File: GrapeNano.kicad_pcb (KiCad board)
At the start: 2 copper layers, 18.3 x 43.7 mm, 31 parts, among them P1 USB_OTG, P2 ICSP, SW1 SW_Push, U1 LM1117-5.0, U2 CH340G, U3 ATMEGA328P-AU, Y1 12MHz, Y2 16Mhz

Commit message: Enrutando
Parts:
- moved F1 6.58 mm to (152.1, 120.6), turned to 90 degrees
- moved Y1 3.54 mm to (160.3, 116.3), turned to 180 degrees
- moved D1 1.78 mm to (154.9, 87.5)
- moved D2 1.78 mm to (156.7, 87.5)
- moved D4 1.78 mm to (160.3, 87.5)
- moved D5 1.78 mm to (158.5, 87.5)
- moved R1 1.78 mm to (154.9, 90.8)
- moved R2 1.78 mm to (156.7, 90.8)
- moved R6 1.78 mm to (160.3, 90.8)
- moved R7 1.78 mm to (158.5, 90.8)
- moved R5 1.53 mm to (161.5, 94.2)
- moved SW1 1.52 mm to (157.5, 94.0)
- moved Y2 0.95 mm to (152.8, 98.4)
- moved P2 0.89 mm to (154.9, 83.8)
- moved D3 0.32 mm to (154.9, 116.4)
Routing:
- net +5V: track 62.2 -> 23.6 mm, vias 3 -> 2
- net A7: track 0.00 -> 27.3 mm
- net D1-TX: track 28.7 -> 8.84 mm, vias 2 -> 0
- net VUSB: track 21.0 -> 7.76 mm, vias 1 -> 0
- net D0-RX: track 20.8 -> 8.86 mm, vias 1 -> 0
- net Net-(C1-Pad2): track 8.67 -> 0.00 mm, vias 2 -> 0
- net GND: track 0.00 -> 8.64 mm, vias 0 -> 3
- net Net-(P1-Pad2): track 9.07 -> 16.5 mm
- net Net-(C6-Pad1): track 17.0 -> 12.3 mm
- net A6: track 0.00 -> 3.25 mm, vias 0 -> 1
- net RESET: track 30.2 -> 33.2 mm
- net DTR: track 2.32 -> 0.00 mm
- net Net-(F1-Pad2): track 5.60 -> 7.73 mm
- net Net-(U2-Pad7): track 2.58 -> 4.55 mm
- net D3: track 9.08 -> 10.8 mm
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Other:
- board size 18.3 x 43.7 mm -> 18.5 x 43.7 mm

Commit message: 4 nets
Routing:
- net D13-SCK: track 11.5 -> 68.0 mm, vias 0 -> 1
- net +5V: track 23.6 -> 71.6 mm, vias 2 -> 4
- net RESET: track 33.2 -> 75.1 mm, vias 0 -> 2
- net D1-TX: track 8.84 -> 46.9 mm, vias 0 -> 1
- net D12-MISO: track 11.6 -> 49.1 mm
- net D11-MOSI: track 9.35 -> 43.6 mm, vias 0 -> 1
- net D0-RX: track 8.86 -> 41.9 mm, vias 0 -> 4
- net VUSB: track 7.76 -> 32.5 mm, vias 0 -> 1
- net GND: track 8.64 -> 33.3 mm, vias 3 -> 12
- net A6: track 3.25 -> 21.8 mm, vias 1 -> 2
- net VIN: track 0.00 -> 15.6 mm
- net Net-(C1-Pad2): track 0.00 -> 8.04 mm
- net Net-(C6-Pad1): track 12.3 -> 18.6 mm
- net DTR: track 0.00 -> 2.32 mm
- net Net-(P1-Pad3): track 9.65 -> 10.6 mm
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
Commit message: enrutando
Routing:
- net (no net): track 0.00 -> 5.44 mm, vias 2 -> 1
- net GND: track 33.3 -> 36.5 mm
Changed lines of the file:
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@@
     (thickness 1.6)
     (drawings 9)
-    (tracks 450)
+    (tracks 458)
     (zones 0)
     (modules 31)
@@
   )
   (via (at 150.622 92.202) (size 0.8) (drill 0.4) (layers F.Cu B.Cu) (net 0))
-  (via (at 151.638 85.598) (size 0.8) (drill 0.4) (layers F.Cu B.Cu) (net 0))
+  (segment (start 156.972 80.01) (end 156.718 80.01) (width 0.25) (layer B.Cu) (net 0))
+  (segment (start 156.718 80.01) (end 157.734 80.01) (width 0.25) (layer B.Cu) (net 0))
+  (segment (start 157.734 80.01) (end 158.242 80.01) (width 0.25) (layer B.Cu) (net 0))
+  (segment (start 156.718 80.01) (end 154.338094 80.01) (width 0.25) (layer B.Cu) (net 0))
+  (segment (start 151.638 87.941002) (end 152.146 88.449002) (width 0.25) (layer B.Cu) (net 0))
+  (segment (start 151.638 85.032315) (end 151.638 85.598) (width 0.25) (layer B.Cu) (net 0))
   (segment (start 160.011861 108.444047) (end 160.782 109.214186) (width 0.25) (layer F.Cu) (net 2) (status 10))
   (segment (start 160.782 109.214186) (end 160.782 109.63868) (width 0.25) (layer F.Cu) (net 2))
@@
   (segment (start 156.755152 96.545152) (end 156.73 96.52) (width 0.25) (layer B.Cu) (net 5))
   (segment (start 157.204846 96.545152) (end 156.755152 96.545152) (width 0.25) (layer B.Cu) (net 5))
+  (segment (start 151.282499 89.371003) (end 151.478001 89.371003) (width 0.25) (layer B.Cu) (net 5))
+  (segment (start 149.637001 91.016501) (end 151.282499 89.371003) (width 0.25) (layer B.Cu) (net 5))
+  (segment (start 151.478001 89.371003) (end 151.954796 88.894208) (width 0.25) (layer B.Cu) (net 5))
   (segment (start 162.274603 106.181305) (end 164.877001 108.783703) (width 0.25) (layer F.Cu) (net 6) (status 30))
   (segment (start 164.877001 108.783703) (end 164.877001 108.796501) (width 0.25) (layer F.Cu) (net 6) (status 30))
@@
   (segment (start 155.69851 109.575417) (end 156.718 108.555927) (width 0.25) (layer F.Cu) (net 40))
   (via (at 156.718 108.458) (size 0.8) (drill 0.4) (layers F.Cu B.Cu) (net 40))
+  (segment (start 152.4 96.208998) (end 152.4 105.935002) (width 0.25) (layer B.Cu) (net 40))
+  (segment (start 152.4 105.935002) (end 153.662997 107.197999) (width 0.25) (layer B.Cu) (net 40))
+  (segment (start 153.662997 107.197999) (end 156.023684 107.197999) (width 0.25) (layer B.Cu) (net 40))
   (segment (start 156.718 107.892315) (end 156.718 108.458) (width 0.25) (layer B.Cu) (net 40))
+  (segment (start 152.146 95.954998) (end 152.4 96.208998) (width 0.25) (layer B.Cu) (net 40))
   (segment (start 156.023684 107.197999) (end 156.718 107.892315) (width 0.25) (layer B.Cu) (net 40))
-  (segment (start 153.662997 107.197999) (end 156.023684 107.197999) (width 0.25) (layer B.Cu) (net 40))
-  (segment (start 152.146 95.954998) (end 152.4 96.208998) (width 0.25) (layer B.Cu) (net 40))
+  (segment (start 152.146 90.678) (end 152.146 95.954998) (width 0.25) (layer B.Cu) (net 40))
   (segment (start 156.215199 86.608801) (end 152.146 90.678) (width 0.25) (layer B.Cu) (net 40))
-  (segment (start 152.4 96.208998) (end 152.4 105.935002) (width 0.25) (layer B.Cu) (net 40))
-  (segment (start 156.215199 82.544801) (end 156.215199 86.608801) (width 0.25) (layer B.Cu) (net 40))
-  (segment (start 152.146 90.678) (end 152.146 95.954998) (width 0.25) (layer B.Cu) (net 40))
-  (segment (start 157.48 81.28) (end 156.215199 82.544801) (width 0.25) (layer B.Cu) (net 40))
-  (segment (start 152.4 105.935002) (end 153.662997 107.197999) (width 0.25) (layer B.Cu) (net 40))
+  (segment (start 156.215199 82.544801) (end 157.48 81.28) (width 0.25) (layer B.Cu) (net 40))
+  (segment (start 156.215199 86.608801) (end 156.215199 82.544801) (width 0.25) (layer B.Cu) (net 40))
   (segment (start 162.1155 106.553) (end 162.2425 106.426) (width 0.25) (layer B.Cu) (net 41))
   (segment (start 160.053 106.553) (end 162.1155 106.553) (width 0.25) (layer B.Cu) (net 41))

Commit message: 1 net
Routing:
- net +5V: track 71.6 -> 81.0 mm, vias 4 -> 2
- net Net-(C6-Pad1): track 18.6 -> 23.9 mm, vias 0 -> 1
- net GND: track 36.5 -> 39.0 mm, vias 12 -> 14
- net (no net): track 5.44 -> 4.16 mm
- net D4: track 10.8 -> 11.9 mm
- net RESET: track 75.1 -> 76.0 mm, vias 2 -> 4

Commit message: Enrutado completo
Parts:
- moved C2 0.51 mm to (157.5, 96.0)
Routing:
- net GND: track 39.0 -> 46.2 mm, vias 14 -> 17
- net +5V: track 81.0 -> 79.5 mm
- net (no net): vias 1 -> 0

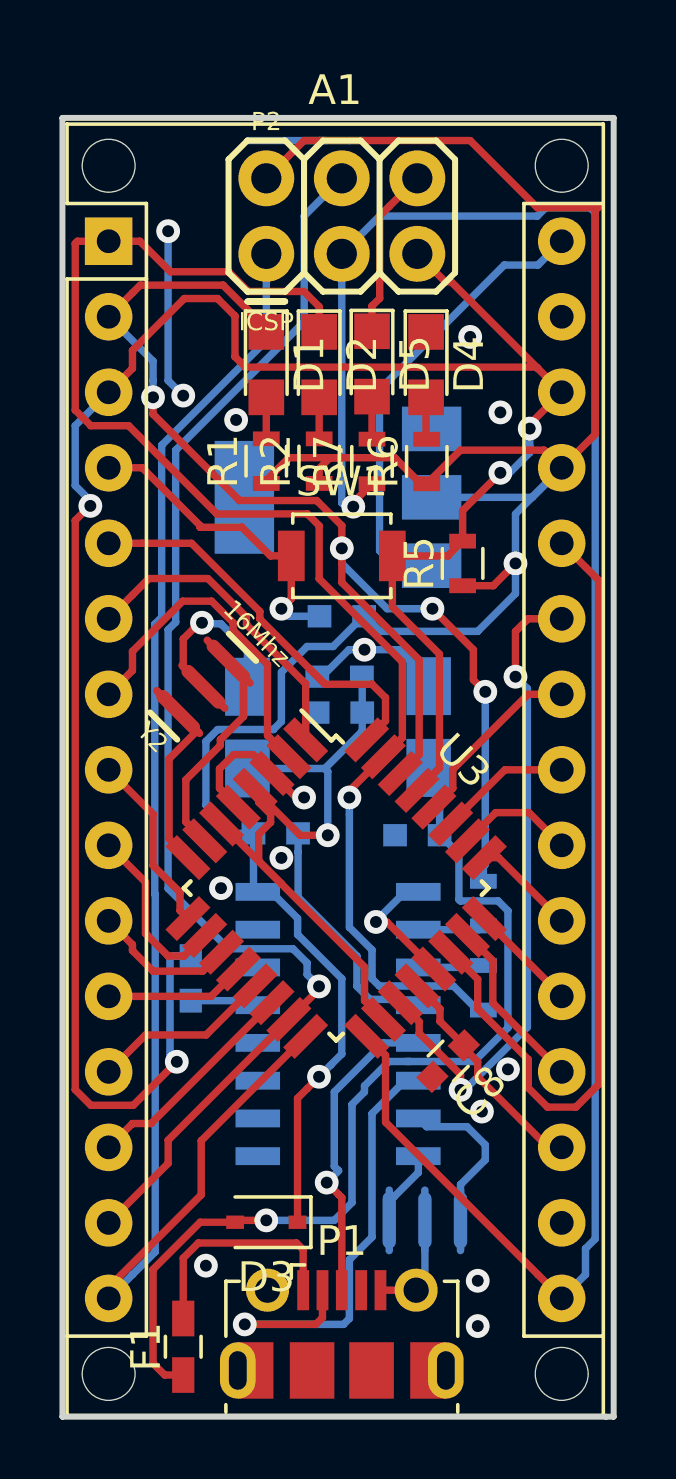
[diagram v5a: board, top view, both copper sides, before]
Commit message: CH340G cambiado por CH340C
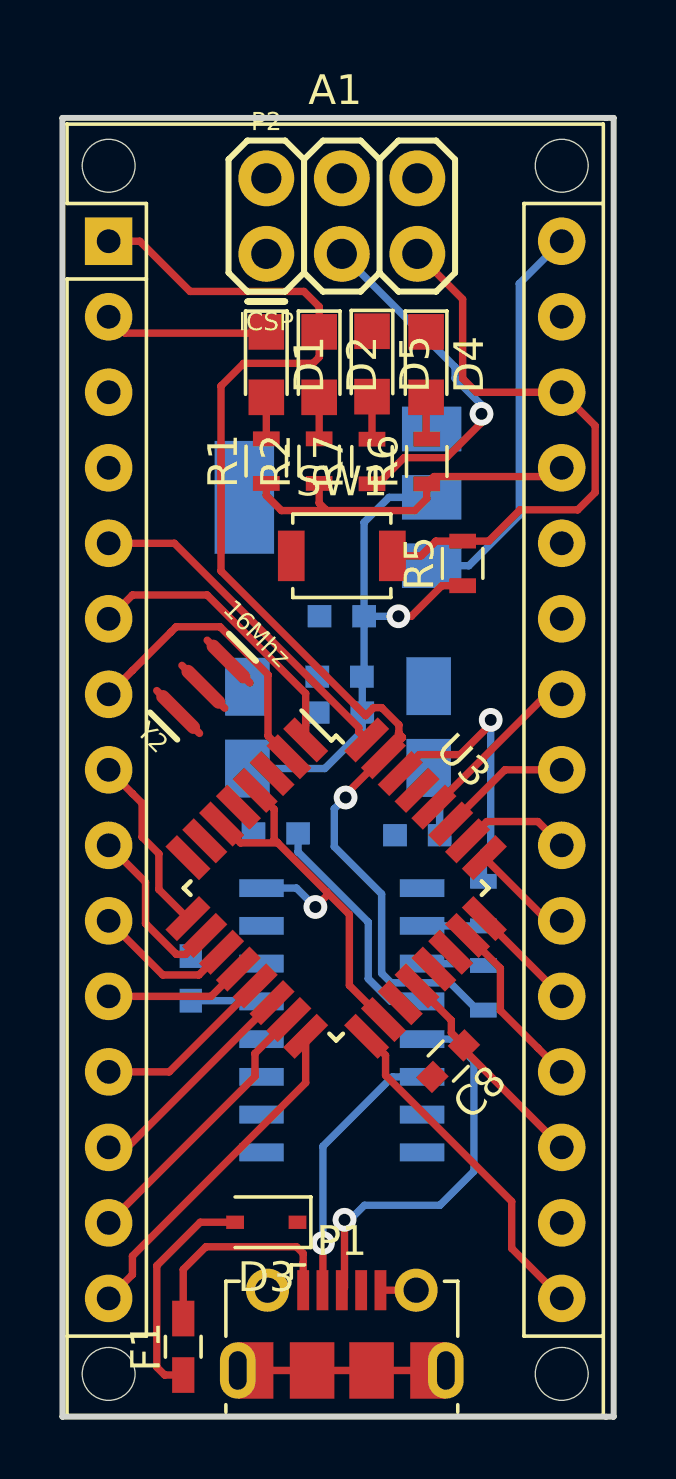
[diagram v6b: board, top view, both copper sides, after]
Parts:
- removed Y1: 12MHz, Clocks:RESONATOR-SMD-3.2X1.3
- U2: value CH340G -> CH340C; footprint Housings_SOIC:SOIC-16_3.9x9.9mm_Pitch1.27mm -> Package_SO:SOIC-16_3.9x9.9mm_P1.27mm
- moved U2 0.18 mm to (157.5, 109.6)
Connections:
- C1 pad 1: +5V -> +3V3
- C6 pad 1: Net-(C6-Pad1) -> +5V
- C7 pad 1: Net-(C6-Pad1) -> +5V
- C9 pad 1: Net-(C6-Pad1) -> +5V
- U3 pad 18: Net-(C6-Pad1) -> +5V
- U3 pad 4: Net-(C6-Pad1) -> +5V
- U3 pad 6: Net-(C6-Pad1) -> +5V
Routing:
- net RESET: track 76.0 -> 19.9 mm, vias 4 -> 0
- net D13-SCK: track 67.8 -> 23.7 mm
- net GND: track 46.2 -> 7.00 mm, vias 17 -> 0
- net D12-MISO: track 48.9 -> 11.6 mm
- net +5V: track 79.5 -> 44.7 mm
- net D11-MOSI: track 43.9 -> 9.35 mm, vias 1 -> 0
- net A7: track 27.3 -> 0.00 mm
- net D0-RX: track 42.1 -> 15.0 mm, vias 4 -> 1
- net Net-(C6-Pad1): track 24.2 -> 0.00 mm, vias 1 -> 0
- net VUSB: track 32.5 -> 10.1 mm, vias 1 -> 0
- net A6: track 22.1 -> 0.00 mm, vias 2 -> 0
- net Net-(P1-Pad2): track 16.5 -> 9.15 mm
- net Net-(U3-Pad7): track 7.31 -> 0.00 mm
- net Net-(U3-Pad8): track 5.90 -> 0.00 mm
- net Net-(U2-Pad7): track 5.51 -> 0.00 mm
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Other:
- net class Default: trace_width 0.25 -> 0.15
- rule trace_min: 0.2 -> 0.125
